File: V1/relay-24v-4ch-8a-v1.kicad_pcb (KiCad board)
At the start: 2 copper layers, 53 x 67.8 mm, 24 parts, among them J1 250-202, J2 250-204, J3 DB142V-5.08-4P, J4 DB142V-5.08-4P, K1 G5Q-1A4-DC24V, K2 G5Q-1A4-DC24V, K3 G5Q-1A4-DC24V, K4 G5Q-1A4-DC24V

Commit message: Replace terminal block
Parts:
- moved R1 3.25 mm to (149.0, 67.0)
- moved R2 3.25 mm to (149.0, 68.5)
- moved R3 3.25 mm to (149.0, 70.0)
- moved R4 3.25 mm to (149.0, 71.5)
- moved J2 3.20 mm to (158.0, 72.5), turned to 180 degrees
- moved J1 2.92 mm to (171.5, 72.5), turned to 180 degrees
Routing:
- net /IN2: track 49.8 -> 32.3 mm
- net /IN1: track 53.1 -> 38.8 mm
- net /IN3: track 48.1 -> 40.5 mm
- net /IN4: track 58.2 -> 51.7 mm
- net +24V: track 111.8 -> 116.5 mm
- net /LED3: track 11.7 -> 8.43 mm
- net /LED2: track 17.6 -> 14.3 mm
- net /LED1: track 23.8 -> 20.5 mm
- net /LED4: track 5.01 -> 1.97 mm
- removed copper zone on F.Cu, net +24V

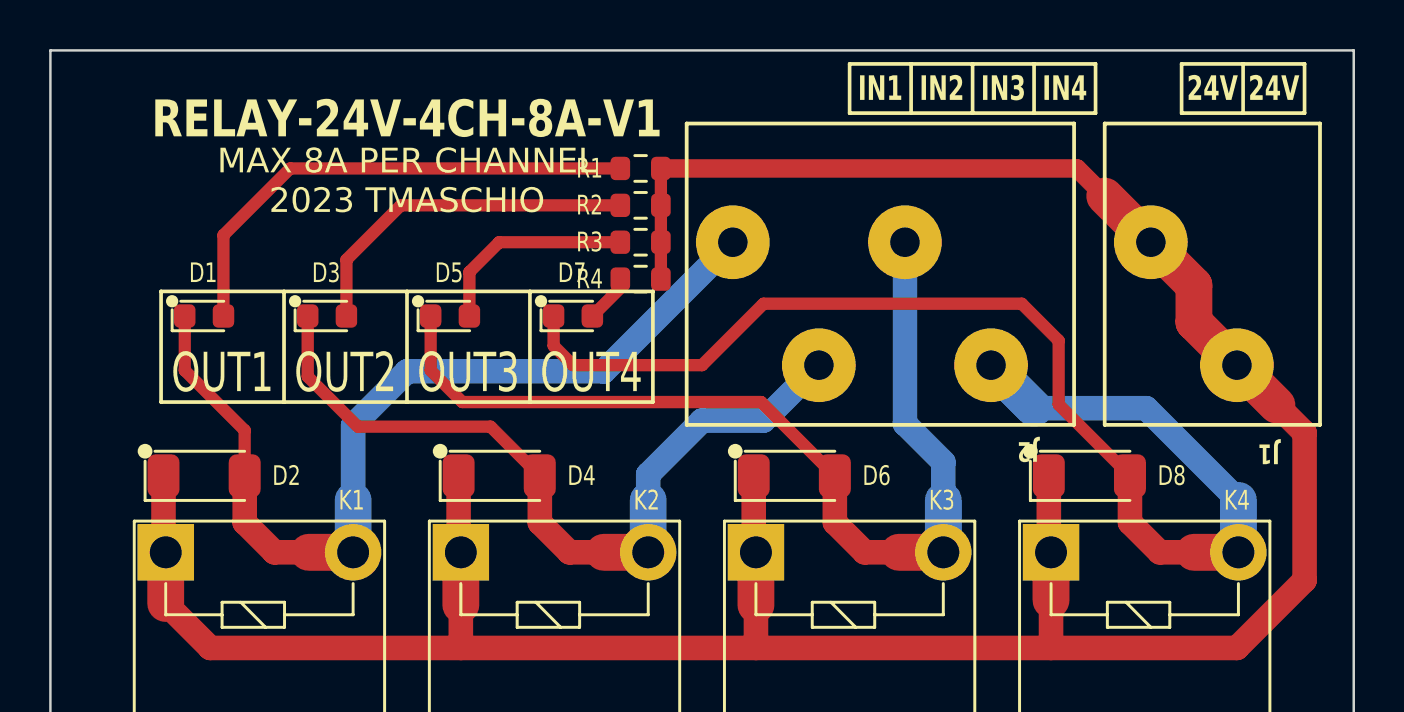
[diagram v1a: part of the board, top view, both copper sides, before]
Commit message: Replaced terminal blocks
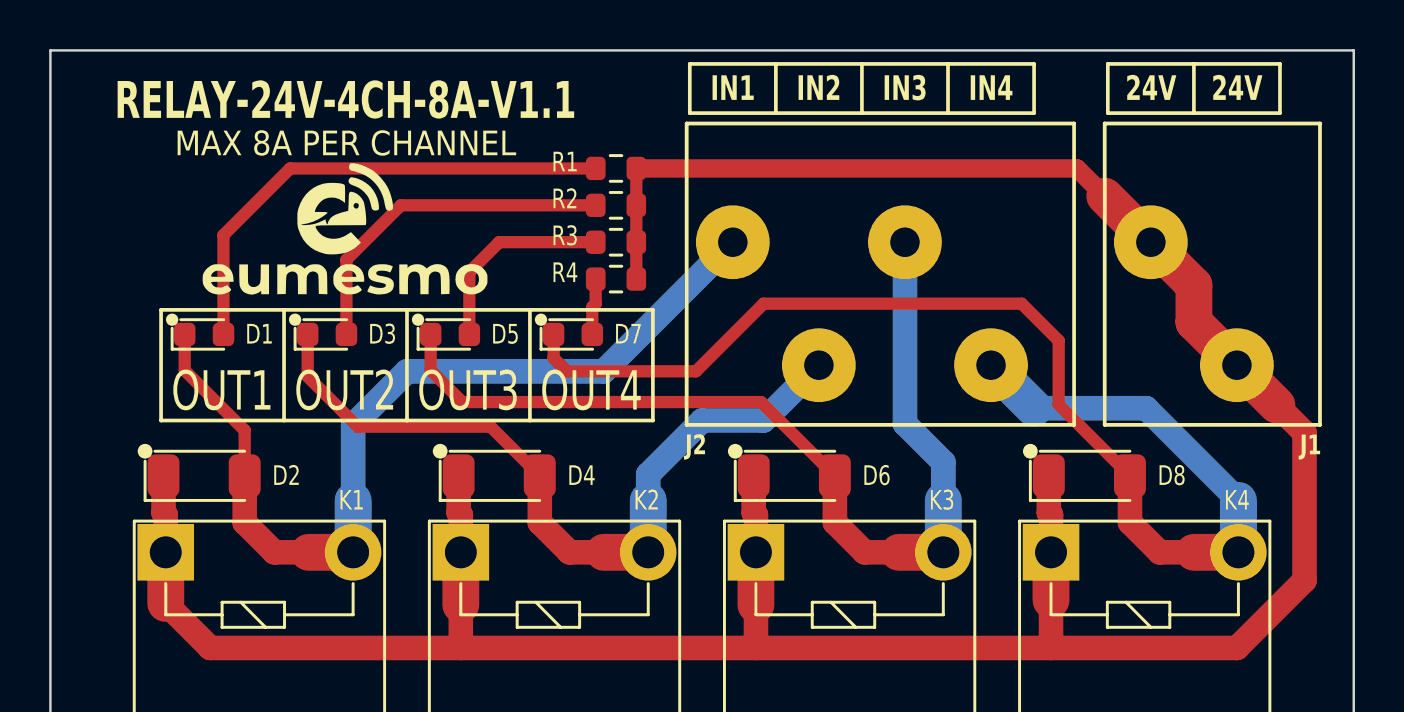
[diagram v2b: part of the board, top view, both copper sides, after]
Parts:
- added G***: LOGO, Tales:Eumesmo_small_silk, F.Cu at (137.0, 69.5)
- moved R1 1.00 mm to (148.0, 67.0)
- moved R2 1.00 mm to (148.0, 68.5)
- moved R3 1.00 mm to (148.0, 70.0)
- moved R4 1.00 mm to (148.0, 71.5)
- moved D1 0.75 mm to (131.2, 73.8)
- moved D3 0.75 mm to (136.2, 73.8)
- moved D5 0.75 mm to (141.2, 73.8)
- moved D7 0.75 mm to (146.2, 73.8)
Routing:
- net /IN1: track 38.8 -> 37.3 mm
- net +24V: track 116.5 -> 117.5 mm
- net /IN3: track 40.5 -> 39.7 mm
- net /IN2: track 32.3 -> 31.6 mm
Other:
- board text added: "MAX 8A PER CHANNEL"
- board text added: "RELAY-24V-4CH-8A-V1.1"
- board text removed: "MAX 8A PER CHANNEL 2023 TMASCHIO"
- board text removed: "RELAY-24V-4CH-8A-V1"
